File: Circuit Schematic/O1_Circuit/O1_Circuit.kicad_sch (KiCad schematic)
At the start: 8 parts, among them U3 L7805

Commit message: Almost finished with Schematic
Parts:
- added D1, D2: D, symbol Device:D
- added Q1, Q2: Q_NMOS, symbol Device:Q_NMOS
- added R1, R2: R-220 Ohm, symbol Device:R
- added R3, R4: R-10K Ohm, symbol Device:R
- C1, C2: value C -> C-10uF
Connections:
- net GND2 is gone; now on net GND: C1.1, C2.1, MCU. (PN4), U3.2 (GND)
- net +12V: now also U1. (GND), U2. (GND), D1.1 (K), D2.1 (K)
- net +5V: now reaches C2.2, Sensors_Left.2 (VCC), Sensors_Right.2 (VCC), U3.3 (OUT)
- net +5V: now also MCU. (PN4)
- net at Sensors_Left.3 (VOUT): now also MCU. (PN4)
- net GND: now reaches U2. (GND)
- net GND: now also U1. (GND), D1.2 (A), D2.2 (A), Q1.D, Q1.S, Q2.D, Q2.S, R3.2, R4.2
- net at Sensors_Right.3 (VOUT): now also MCU. (PN4)
- new net: MCU. (PN4), R1.1
- new net: MCU. (PN4), R2.1
- new net: Q1.G, R1.2, R4.1
- new net: Q2.G, R2.2, R3.1
- no-connect marks 0 -> 74

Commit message: Begin Prototyping
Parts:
- added U4: CRE1S1205SC, Converter_DCDC:Converter_DCDC_Murata_CRE1xxxxxxSC_THT, symbol Regulator_Switching:CRE1S1205SC
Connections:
- net +12V: now also U4.2 (+VIN); no longer D1.1 (K), D2.1 (K), U1. (GND), U2. (GND)
- net GND: now also U4.1 (-VIN); no longer D1.2 (A), D2.2 (A), Q1.D, Q1.S, Q2.D, Q2.S, R3.2, R4.2, U1. (GND), U2. (GND)
- net at Sensors_Left.1 (GND), Sensors_Right.1 (GND): now also MCU. (PN4)
- net at MCU. (PN4), Sensors_Left.3 (VOUT): now also R1.1
- new net: D1.1 (K), D2.1 (K), U1. (GND), U2. (GND), U4.4 (+VOUT)
- new net: D1.2 (A), Q2.D, U2. (GND)
- new net: D2.2 (A), Q1.D, U1. (GND)
- new net: Q1.S, Q2.S, R3.2, R4.2, U4.3 (-VOUT)
- no-connect marks 74 -> 73

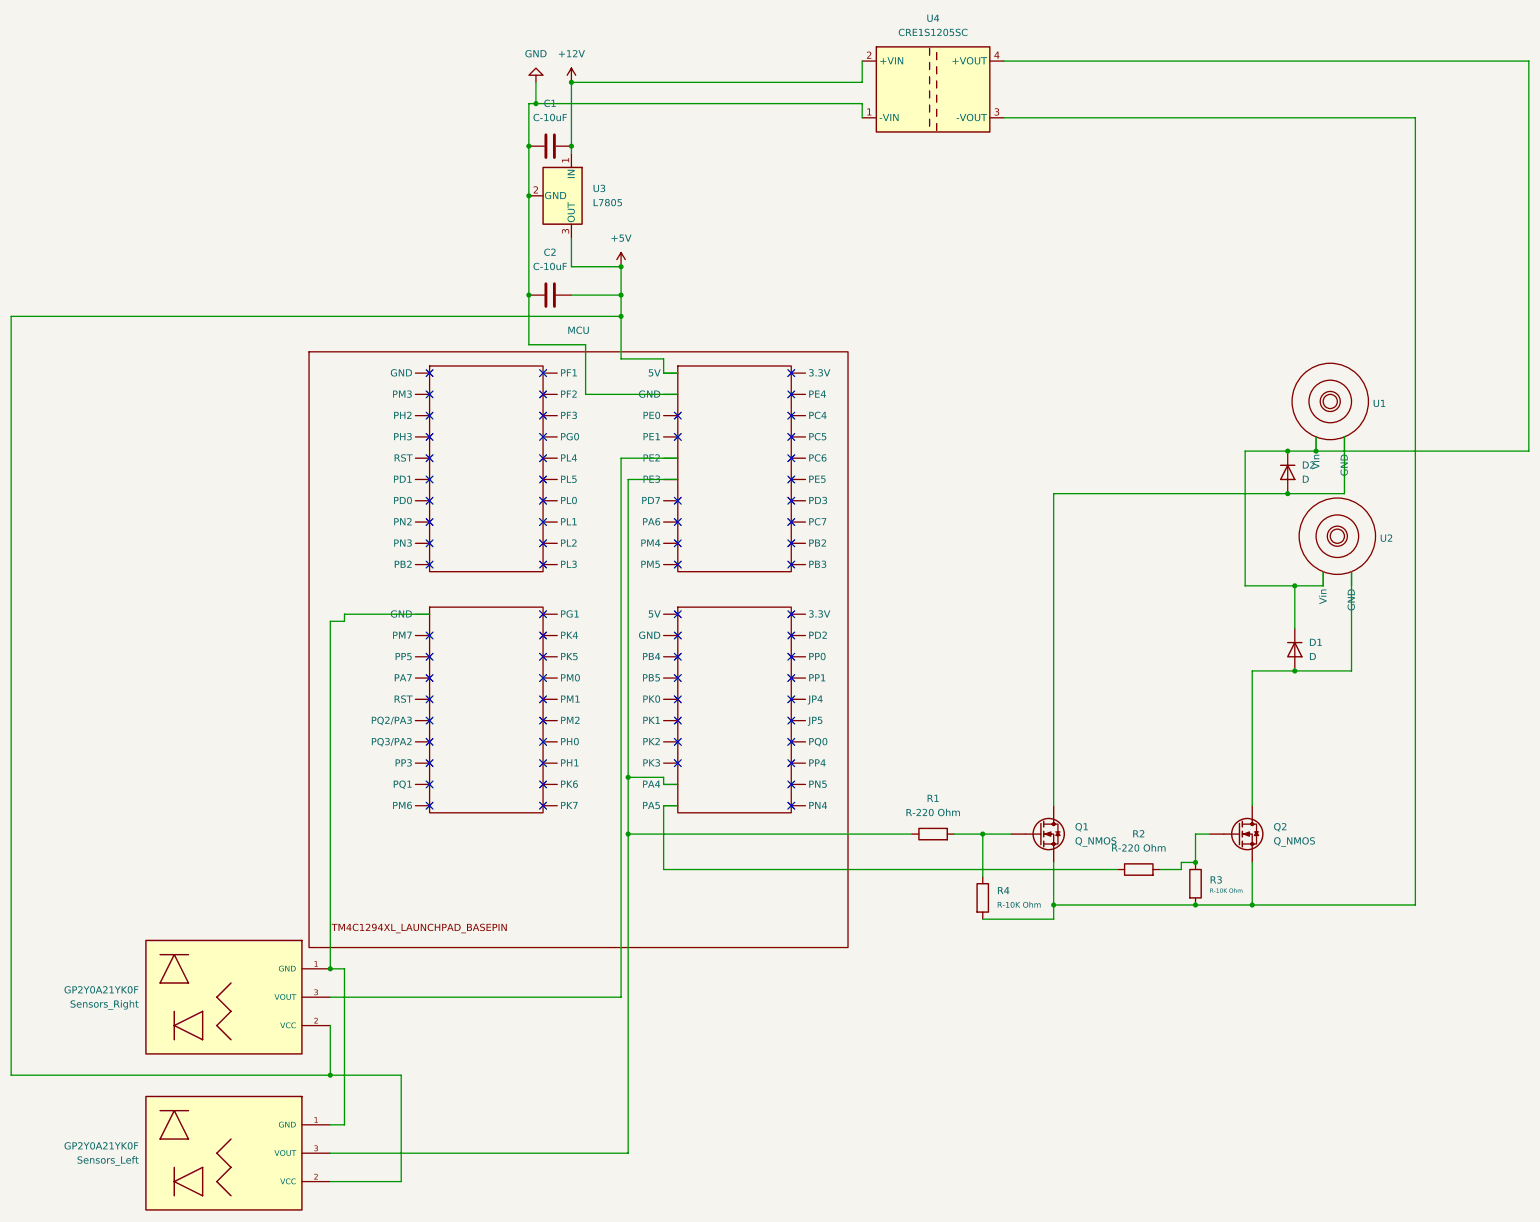
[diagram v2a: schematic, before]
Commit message: Fixing Schematic and Start desigbing PCB
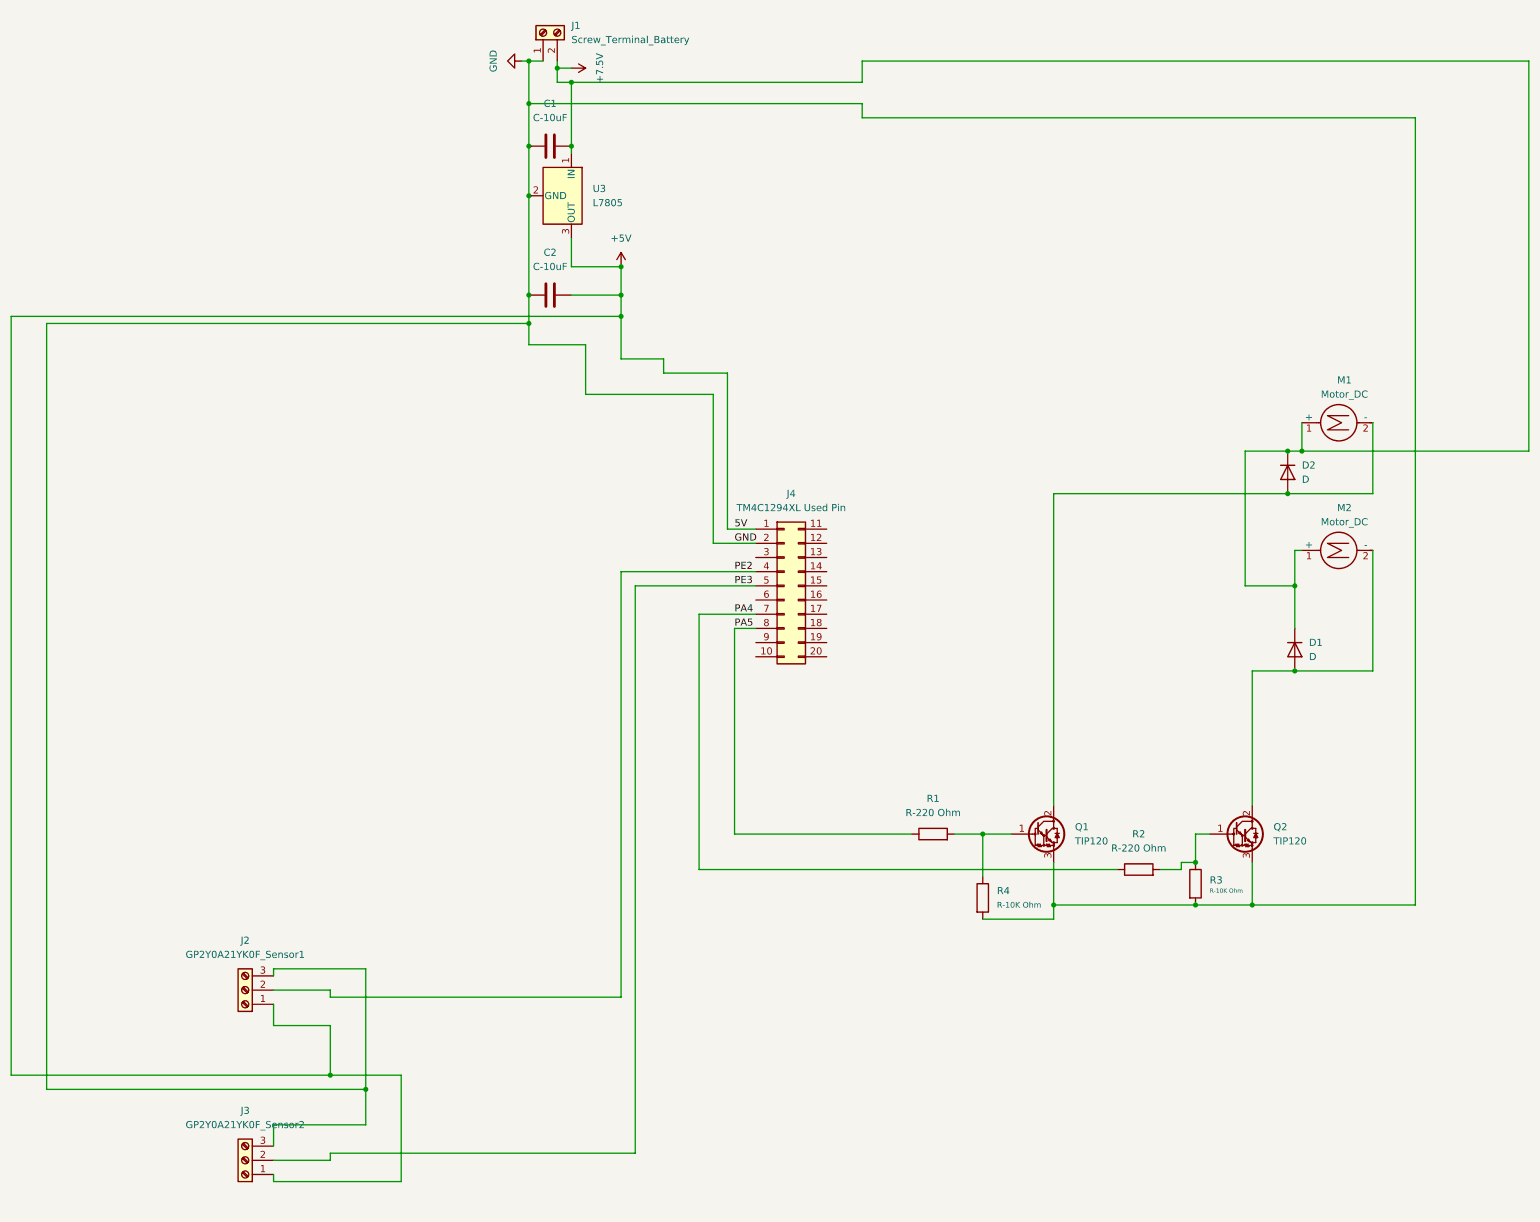
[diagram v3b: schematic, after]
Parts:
- removed MCU: ~, symbol TM4C1294XL_LaunchPad_Base:TM4C_LAUNCHPAD
- removed Q1, Q2: Q_NMOS, symbol Device:Q_NMOS
- removed Sensors_Left, Sensors_Right: GP2Y0A21YK0F, GP2Y0A21YK0F:22-23-2031, symbol GP2Y0A21YK0F:GP2Y0A21YK0F
- removed U1, U2: ~, symbol DCMOTOR_5-12V_F130:DCMOTOR_5-12V_F130
- removed U4: CRE1S1205SC, Converter_DCDC:Converter_DCDC_Murata_CRE1xxxxxxSC_THT, symbol Regulator_Switching:CRE1S1205SC
- added J1: Screw_Terminal_Battery, TerminalBlock_Phoenix:TerminalBlock_Phoenix_MPT-0,5-2-2.54_1x02_P2.54mm_Horizontal, symbol Connector:Screw_Terminal_01x02
- added J2: GP2Y0A21YK0F_Sensor1, TerminalBlock_Phoenix:TerminalBlock_Phoenix_MPT-0,5-3-2.54_1x03_P2.54mm_Horizontal, symbol Connector:Screw_Terminal_01x03
- added J3: GP2Y0A21YK0F_Sensor2, TerminalBlock_Phoenix:TerminalBlock_Phoenix_MPT-0,5-3-2.54_1x03_P2.54mm_Horizontal, symbol Connector:Screw_Terminal_01x03
- added J4: TM4C1294XL Used Pin, Connector_PinHeader_2.54mm:PinHeader_2x10_P2.54mm_Vertical, symbol Connector_Generic:Conn_02x10_Top_Bottom
- added M1, M2: Motor_DC, TerminalBlock_Phoenix:TerminalBlock_Phoenix_MPT-0,5-2-2.54_1x02_P2.54mm_Horizontal, symbol Motor:Motor_DC
- added Q1, Q2: TIP120, Package_TO_SOT_THT:TO-220-3_Vertical, symbol Transistor_BJT:TIP120
- C1, C2: footprint (none) -> Capacitor_SMD:C_0805_2012Metric
- D1, D2: footprint (none) -> Diode_THT:D_A-405_P2.54mm_Vertical_AnodeUp
- R1, R2, R3, R4: footprint (none) -> Resistor_THT:R_Axial_DIN0207_L6.3mm_D2.5mm_P7.62mm_Horizontal
- U3: footprint (none) -> Package_TO_SOT_THT:TO-220-3_Vertical
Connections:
- net +12V is gone; now on net +7.5V: C1.2, U3.1 (IN)
- net +5V: now also J2.1 (Pin_1), J3.1 (Pin_1), J4.1 (Pin_1)
- net GND: now also R3.2, R4.2, J1.1 (Pin_1), J2.3 (Pin_3), J3.3 (Pin_3), J4.2 (Pin_2), Q1.3 (E), Q2.3 (E)
- net PA5: now reaches R1.1
- net PA5: now also J4.8 (Pin_8)
- net +7.5V: now reaches D1.1 (K), D2.1 (K)
- net +7.5V: now also J1.2 (Pin_2), M1.1 (+), M2.1 (+)
- net at D1.2 (A): now also M2.2 (-), Q2.2 (C)
- net PA4: now reaches R2.1
- net PA4: now also J4.7 (Pin_7)
- net at D2.2 (A): now also M1.2 (-), Q1.2 (C)
- net at R1.2, R4.1: now also Q1.1 (B)
- net at R2.2, R3.1: now also Q2.1 (B)
- new net PE2: J2.2 (Pin_2), J4.4 (Pin_4)
- new net PE3: J3.2 (Pin_2), J4.5 (Pin_5)
- no-connect marks 73 -> 0

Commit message: Fiishing PCB
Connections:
- no-connect marks 0 -> 14
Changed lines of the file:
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@@
 		(color 0 0 0 0)
+	)
+	(no_connect
+		(at 208.28 120.65)
+	)
+	(no_connect
+		(at 208.28 123.19)
+	)
+	(no_connect
+		(at 208.28 125.73)
+	)
+	(no_connect
+		(at 195.58 143.51)
+	)
+	(no_connect
+		(at 195.58 140.97)
+	)
+	(no_connect
+		(at 208.28 128.27)
+	)
+	(no_connect
+		(at 195.58 125.73)
+	)
+	(no_connect
+		(at 208.28 130.81)
+	)
+	(no_connect
+		(at 208.28 140.97)
+	)
+	(no_connect
+		(at 208.28 138.43)
+	)
+	(no_connect
+		(at 208.28 135.89)
+	)
+	(no_connect
+		(at 208.28 133.35)
+	)
+	(no_connect
+		(at 208.28 143.51)
+	)
+	(no_connect
+		(at 195.58 133.35)
 	)
 	(wire

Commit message: PCB Design Edit
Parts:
- added H1, H2, H3, H4: MountingHole, MountingHole:MountingHole_2.5mm, symbol Mechanical:MountingHole

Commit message: Editing PCB due to short on prev
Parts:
- C1, C2: footprint Capacitor_SMD:C_0805_2012Metric -> Capacitor_THT:C_Disc_D7.5mm_W5.0mm_P5.00mm
- J1, M1, M2: footprint TerminalBlock_Phoenix:TerminalBlock_Phoenix_MPT-0,5-2-2.54_1x02_P2.54mm_Horizontal -> TerminalBlock_Phoenix:TerminalBlock_Phoenix_MKDS-3-2-5.08_1x02_P5.08mm_Horizontal
- J2, J3: footprint TerminalBlock_Phoenix:TerminalBlock_Phoenix_MPT-0,5-3-2.54_1x03_P2.54mm_Horizontal -> TerminalBlock_Phoenix:TerminalBlock_Phoenix_MKDS-3-3-5.08_1x03_P5.08mm_Horizontal
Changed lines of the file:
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@@
 			)
 		)
-		(property "Footprint" "Capacitor_SMD:C_0805_2012Metric"
+		(property "Footprint" "Capacitor_THT:C_Disc_D7.5mm_W5.0mm_P5.00mm"
 			(at 162.56 51.1048 0)
 			(effects
@@
 			)
 		)
-		(property "Footprint" "TerminalBlock_Phoenix:TerminalBlock_Phoenix_MPT-0,5-2-2.54_1x02_P2.54mm_Horizontal"
+		(property "Footprint" "TerminalBlock_Phoenix:TerminalBlock_Phoenix_MKDS-3-2-5.08_1x02_P5.08mm_Horizontal"
 			(at 157.48 31.75 0)
 			(effects
@@
 			)
 		)
-		(property "Footprint" "TerminalBlock_Phoenix:TerminalBlock_Phoenix_MPT-0,5-2-2.54_1x02_P2.54mm_Horizontal"
+		(property "Footprint" "TerminalBlock_Phoenix:TerminalBlock_Phoenix_MKDS-3-2-5.08_1x02_P5.08mm_Horizontal"
 			(at 300.736 101.6 0)
 			(effects
@@
 			)
 		)
-		(property "Footprint" "TerminalBlock_Phoenix:TerminalBlock_Phoenix_MPT-0,5-2-2.54_1x02_P2.54mm_Horizontal"
+		(property "Footprint" "TerminalBlock_Phoenix:TerminalBlock_Phoenix_MKDS-3-2-5.08_1x02_P5.08mm_Horizontal"
 			(at 300.736 124.46 0)
 			(effects
@@
 			)
 		)
-		(property "Footprint" "TerminalBlock_Phoenix:TerminalBlock_Phoenix_MPT-0,5-3-2.54_1x03_P2.54mm_Horizontal"
+		(property "Footprint" "TerminalBlock_Phoenix:TerminalBlock_Phoenix_MKDS-3-3-5.08_1x03_P5.08mm_Horizontal"
 			(at 104.14 233.68 0)
 			(effects
@@
 			)
 		)
-		(property "Footprint" "Capacitor_SMD:C_0805_2012Metric"
+		(property "Footprint" "Capacitor_THT:C_Disc_D7.5mm_W5.0mm_P5.00mm"
 			(at 162.56 77.7748 0)
 			(effects
@@
 			)
 		)
-		(property "Footprint" "TerminalBlock_Phoenix:TerminalBlock_Phoenix_MPT-0,5-3-2.54_1x03_P2.54mm_Horizontal"
+		(property "Footprint" "TerminalBlock_Phoenix:TerminalBlock_Phoenix_MKDS-3-3-5.08_1x03_P5.08mm_Horizontal"
 			(at 104.14 203.2 0)
 			(effects
